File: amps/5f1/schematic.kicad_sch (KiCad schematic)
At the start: 26 parts, among them T2 SE 5k:8

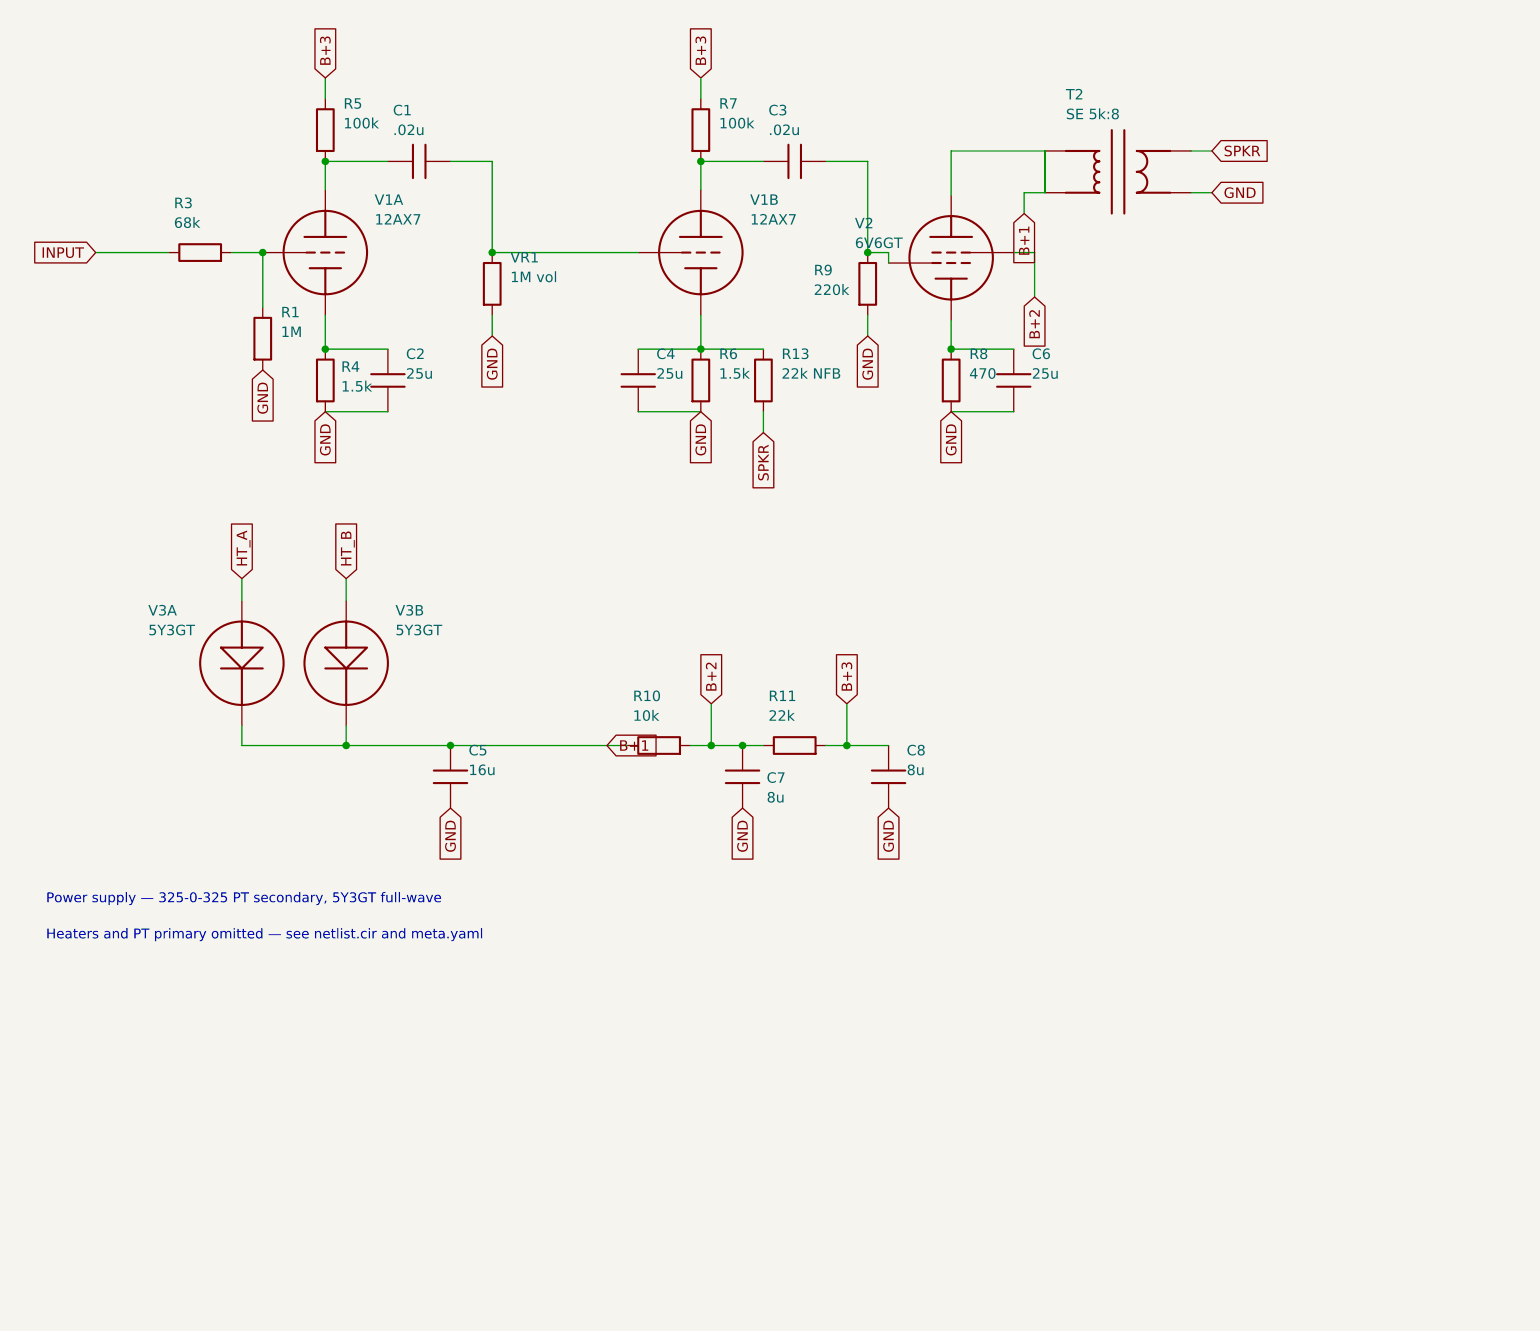
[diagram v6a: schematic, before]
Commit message: Add: real tube pin numbers and readable valve glyphs on every schematic
Phase B of the drawing program. A factory service sheet numbers every tube
pin, because the number is what a technician puts a probe on. This corpus
printed none, and the numbers hidden in its symbols were positional
placeholders (P=1, G=2, K=3) that would have published a 6V6GT's plate as
pin 1 when it is pin 3.

1055 electrodes now carry the real number, 1027 lettered (27 are shared
filaments deduped, 1 dropped for want of clear space on the 6G2). Resolved per
instance from reference/tubes/<slug>.yaml through the same alias resolution the
layout renderer uses, so a 12AX7 section and a 6SL7 section each get their own
basing. A valve whose basing the corpus does not carry prints nothing rather
than a wrong number.

Section letters and basing units are now separate things, which cost a detour
worth recording. The RCA 12AX7-A sheet reads "Pin 1 - Plate of Unit No.2 ...
Pin 6 - Plate of Unit No.1", so unit numbering is not pin order; the 5Y3 and
GZ34 number their units in opposite pin order, so nothing positional can
express it. But the section LETTER is a designator, not a basing fact: this
corpus, like every technician, calls the first stage in signal order V1A, and
five amps' prose already did. On four amps the factory sheets put that first
stage on the other half -- the AA764's own schematic prints +200 V on pin 1 --
so those drawings now state their unit explicitly, each citing its source, and
no letter, netlist, parts list or layout comment changed. 183 layout comments
agree with the printed numbers, 0 disagree. A guard fires if two halves of one
bottle resolve to the same unit, which is exactly how this was found.

Glyphs: the cathode gains a bracket and filament hairpin so it can no longer be
confused with the plate bar, the pentode's screen sits on its own row, and a
rectifier draws as one envelope over its sections instead of two apparent
bottles. Line weights are scaled per sheet to a co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
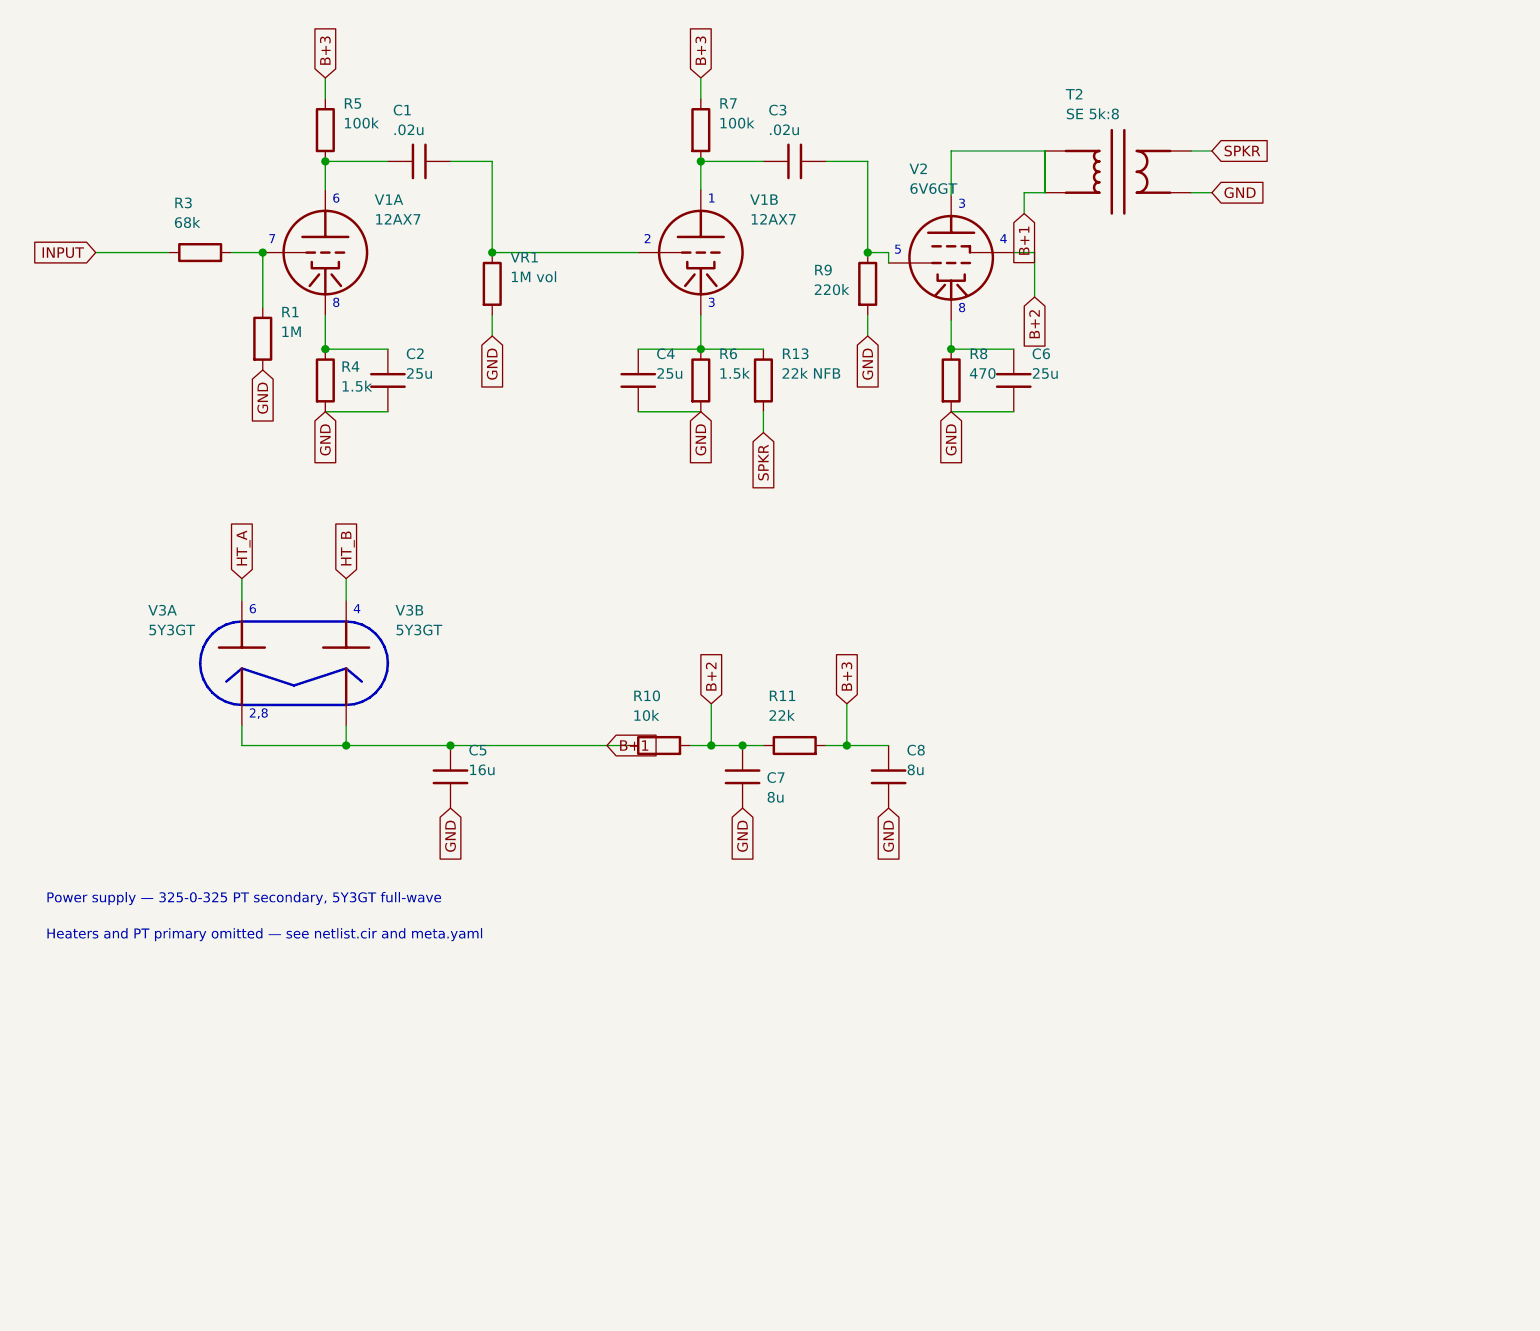
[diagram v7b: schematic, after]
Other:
- note added: "1"
- note added: "2"
- note added: "2,8"
- note added: "3"
- note added: "4"
- note added: "5"
- note added: "6"
- note added: "7"
- note added: "8"
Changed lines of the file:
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@@
     (property "Reference" "V1A" (at 52.7052 31.878 0) (effects (font (size 1.27 1.27)) (justify left)))
     (property "Value" "12AX7" (at 52.7052 34.278 0) (effects (font (size 1.27 1.27)) (justify left))))
-  (junction (at 39.0852 38.278) (diameter 0) (color 0 0 0 0))
+  (junction (at 39.0852 38.278) (diameter 1) (color 0 0 0 0))
   (symbol (lib_id "cx:R") (at 39.0852 48.768 0) (unit 1)
     (in_bom yes) (on_board yes)
@@
   (wire (pts (xy 46.7052 45.898) (xy 46.7052 50.038))
     (stroke (width 0) (type default)))
-  (junction (at 46.7052 50.038) (diameter 0) (color 0 0 0 0))
+  (junction (at 46.7052 50.038) (diameter 1) (color 0 0 0 0))
   (symbol (lib_id "cx:R") (at 46.7052 53.848 0) (unit 1)
     (in_bom yes) (on_board yes)
@@
   (wire (pts (xy 46.7052 30.658) (xy 46.7052 27.178))
     (stroke (width 0) (type default)))
-  (junction (at 46.7052 27.178) (diameter 0) (color 0 0 0 0))
+  (junction (at 46.7052 27.178) (diameter 1) (color 0 0 0 0))
   (symbol (lib_id "cx:R") (at 46.7052 23.368 0) (unit 1)
     (in_bom yes) (on_board yes)
@@
   (wire (pts (xy 67.0252 27.178) (xy 67.0252 38.278))
     (stroke (width 0) (type default)))
-  (junction (at 67.0252 38.278) (diameter 0) (color 0 0 0 0))
+  (junction (at 67.0252 38.278) (diameter 1) (color 0 0 0 0))
   (symbol (lib_id "cx:R") (at 67.0252 42.088 0) (unit 1)
     (in_bom yes) (on_board yes)
@@
   (wire (pts (xy 92.4252 45.898) (xy 92.4252 50.038))
     (stroke (width 0) (type default)))
-  (junction (at 92.4252 50.038) (diameter 0) (color 0 0 0 0))
+  (junction (at 92.4252 50.038) (diameter 1) (color 0 0 0 0))
   (symbol (lib_id "cx:R") (at 92.4252 53.848 0) (unit 1)
     (in_bom yes) (on_board yes)
@@
   (wire (pts (xy 92.4252 30.658) (xy 92.4252 27.178))
     (stroke (width 0) (type default)))
-  (junction (at 92.4252 27.178) (diameter 0) (color 0 0 0 0))
+  (junction (at 92.4252 27.178) (diameter 1) (color 0 0 0 0))
   (symbol (lib_id "cx:R") (at 92.4252 23.368 0) (unit 1)
     (in_bom yes) (on_board yes)
@@
   (wire (pts (xy 112.745 27.178) (xy 112.745 38.278))
     (stroke (width 0) (type default)))
-  (junction (at 112.745 38.278) (diameter 0) (color 0 0 0 0))
+  (junction (at 112.745 38.278) (diameter 1) (color 0 0 0 0))
   (symbol (lib_id "cx:R") (at 112.745 42.088 0) (unit 1)
     (in_bom yes) (on_board yes)
@@
   (symbol (lib_id "cx:PENTODE") (at 122.905 38.913 0) (unit 1)
     (in_bom yes) (on_board yes)
-    (property "Reference" "V2" (at 111.181 34.733 0) (effects (font (size 1.27 1.27)) (justify left)))
-    (property "Value" "6V6GT" (at 111.181 37.133 0) (effects (font (size 1.27 1.27)) (justify left))))
+    (property "Reference" "V2" (at 117.825 28.133 0) (effects (font (size 1.27 1.27)) (justify left)))
+    (property "Value" "6V6GT" (at 117.825 30.533 0) (effects (font (size 1.27 1.27)) (justify left))))
   (wire (pts (xy 115.285 38.278) (xy 115.285 39.548))
     (stroke (width 0) (type default)))
@@
   (wire (pts (xy 122.905 46.533) (xy 122.905 50.038))
     (stroke (width 0) (type default)))
-  (junction (at 122.905 50.038) (diameter 0) (color 0 0 0 0))
+  (junction (at 122.905 50.038) (diameter 1) (color 0 0 0 0))
   (symbol (lib_id "cx:R") (at 122.905 53.848 0) (unit 1)
     (in_bom yes) (on_board yes)
@@
   (wire (pts (xy 61.9452 98.298) (xy 80.9952 98.298))
     (stroke (width 0) (type default)))
-  (junction (at 49.2452 98.298) (diameter 0) (color 0 0 0 0))
-  (junction (at 61.9452 98.298) (diameter 0) (color 0 0 0 0))
+  (junction (at 49.2452 98.298) (diameter 1) (color 0 0 0 0))
+  (junction (at 61.9452 98.298) (diameter 1) (color 0 0 0 0))
   (symbol (lib_id "cx:C") (at 61.9452 102.108 0) (unit 1)
     (in_bom yes) (on_board yes)
@@
   (wire (pts (xy 97.5052 98.298) (xy 100.045 98.298))
     (stroke (width 0) (type default)))
-  (junction (at 93.6952 98.298) (diameter 0) (color 0 0 0 0))
+  (junction (at 93.6952 98.298) (diameter 1) (color 0 0 0 0))
   (global_label "B+2" (shape input) (at 93.6952 93.218 90)
     (effects (font (size 1.27 1.27)) (justify left)))
   (wire (pts (xy 93.6952 93.218) (xy 93.6952 98.298))
     (stroke (width 0) (type default)))
-  (junction (at 97.5052 98.298) (diameter 0) (color 0 0 0 0))
+  (junction (at 97.5052 98.298) (diameter 1) (color 0 0 0 0))
   (symbol (lib_id "cx:C") (at 97.5052 102.108 0) (unit 1)
     (in_bom yes) (on_board yes)
@@
   (wire (pts (xy 110.205 98.298) (xy 115.285 98.298))
     (stroke (width 0) (type default)))
-  (junction (at 110.205 98.298) (diameter 0) (color 0 0 0 0))
+  (junction (at 110.205 98.298) (diameter 1) (color 0 0 0 0))
   (global_label "B+3" (shape input) (at 110.205 93.218 90)
     (effects (font (size 1.27 1.27)) (justify left)))
@@
   (global_label "GND" (shape input) (at 115.285 105.918 270)
     (effects (font (size 1.27 1.27)) (justify right)))
+  (polyline (pts (xy 49.2452 83.198) (xy 50.2362 83.296) (xy 51.1892 83.585) (xy 52.0672 84.054) (xy 52.8372 84.686) (xy 53.4692 85.456) (xy 53.9382 86.334) (xy 54.2272 87.287) (xy 54.3252 88.278) (xy 54.2272 89.269) (xy 53.9382 90.222) (xy 53.4692 91.1) (xy 52.8372 91.87) (xy 52.0672 92.502) (xy 51.1892 92.971) (xy 50.2362 93.26) (xy 49.2452 93.358) (xy 36.5452 93.358) (xy 35.5542 93.26) (xy 34.6012 92.971) (xy 33.7232 92.502) (xy 32.9532 91.87) (xy 32.3212 91.1) (xy 31.8522 90.222) (xy 31.5632 89.269) (xy 31.4652 88.278) (xy 31.5632 87.287) (xy 31.8522 86.334) (xy 32.3212 85.456) (xy 32.9532 84.686) (xy 33.7232 84.054) (xy 34.6012 83.585) (xy 35.5542 83.296) (xy 36.5452 83.198) (xy 49.2452 83.198))
+    (stroke (width 0.3) (type default) (color 197 163 255 1)) (fill (type none)))
+  (polyline (pts (xy 34.6452 90.513) (xy 36.5452 88.913) (xy 42.8952 90.993) (xy 49.2452 88.913) (xy 51.1452 90.513))
+    (stroke (width 0.3) (type default) (color 197 163 255 1)) (fill (type none)))
+  (text "6" (at 47.5552 31.928 0)
+    (effects (font (size 1.1 1.1)) (justify left)))
+  (text "7" (at 39.758 36.878 0)
+    (effects (font (size 1.1 1.1)) (justify left)))
+  (text "8" (at 47.5552 44.628 0)
+    (effects (font (size 1.1 1.1)) (justify left)))
+  (text "1" (at 93.2752 31.928 0)
+    (effects (font (size 1.1 1.1)) (justify left)))
+  (text "2" (at 85.478 36.878 0)
+    (effects (font (size 1.1 1.1)) (justify left)))
+  (text "3" (at 93.2752 44.628 0)
+    (effects (font (size 1.1 1.1)) (justify left)))
+  (text "3" (at 123.755 32.563 0)
+    (effects (font (size 1.1 1.1)) (justify left)))
+  (text "5" (at 115.958 38.148 0)
+    (effects (font (size 1.1 1.1)) (justify left)))
+  (text "4" (at 128.805 36.878 0)
+    (effects (font (size 1.1 1.1)) (justify left)))
+  (text "8" (at 123.755 45.263 0)
+    (effects (font (size 1.1 1.1)) (justify left)))
+  (text "6" (at 37.3952 81.928 0)
+    (effects (font (size 1.1 1.1)) (justify left)))
+  (text "2,8" (at 37.3952 94.628 0)
+    (effects (font (size 1.1 1.1)) (justify left)))
+  (text "4" (at 50.0952 81.928 0)
+    (effects (font (size 1.1 1.1)) (justify left)))
   (text "Power supply — 325-0-325 PT secondary, 5Y3GT full-wave" (at 12.7 117.076 0)
     (effects (font (size 1.2 1.2)) (justify left)))
